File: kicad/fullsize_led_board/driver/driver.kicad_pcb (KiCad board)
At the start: 2 copper layers, 163.5 x 127.5 mm, 131 parts, among them J4 Anodes Header, J5 Cathodes Header, Q1 SQ2351CES, Q10 SQ2351CES, Q11 SQ2351CES, Q12 SQ2351CES, Q13 SQ2351CES, Q14 SQ2351CES, Q15 SQ2351CES, Q16 SQ2351CES, Q17 SQ2351CES, Q18 SQ2351CES, Q19 SQ2351CES, Q2 SQ2351CES, Q20 SQ2351CES, Q21 SQ2351CES, Q22 SQ2351CES, Q23 SQ2351CES, Q24 SQ2351CES, Q3 SQ2351CES, Q4 SQ2351CES, Q5 SQ2351CES, Q6 SQ2351CES, Q7 SQ2351CES, Q8 SQ2351CES, Q9 SQ2351CES, U1 74HCT541, U2 74HCT595, U3 74HCT595, U4 74HCT595, U5 TPIC6B595N, U6 TPIC6B595N, U7 TPIC6B595N, U8 TPIC6B595N

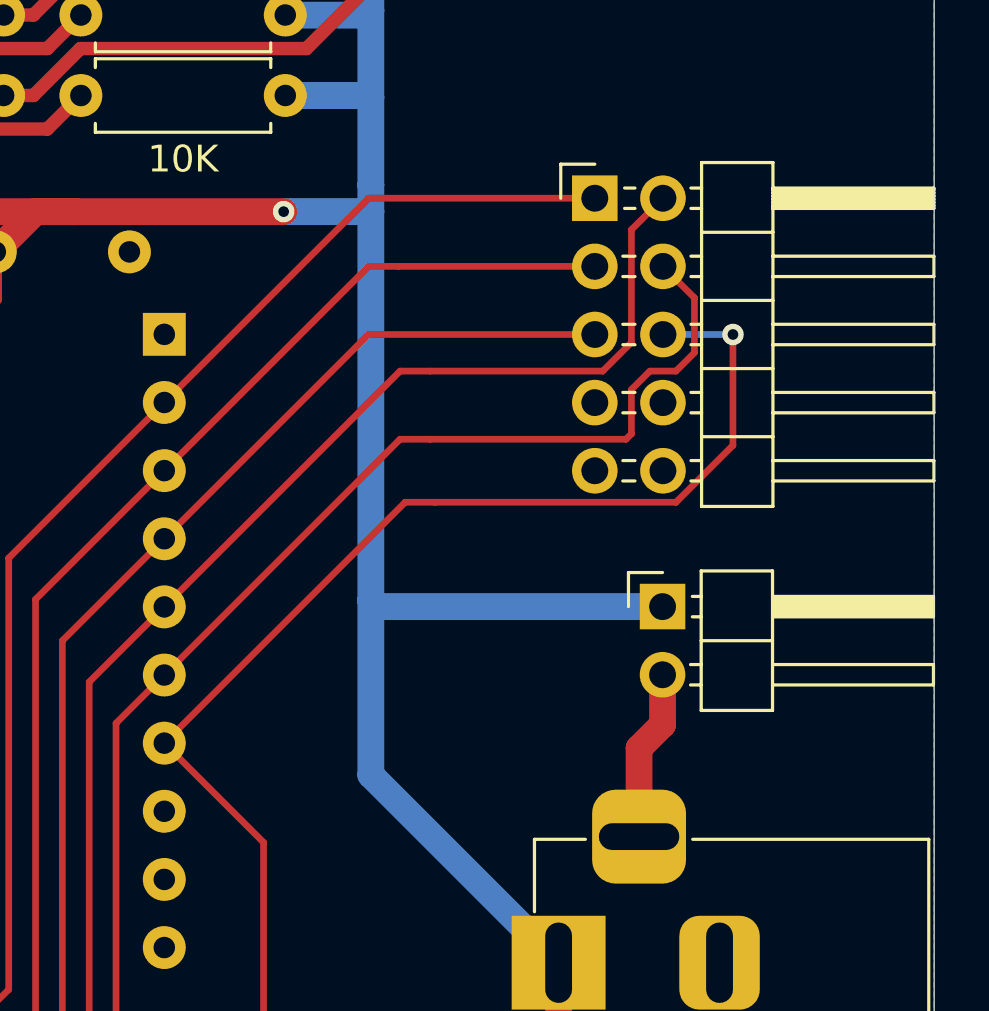
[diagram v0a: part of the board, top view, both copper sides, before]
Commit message: fullsize led board: done, inspection now and then ordering
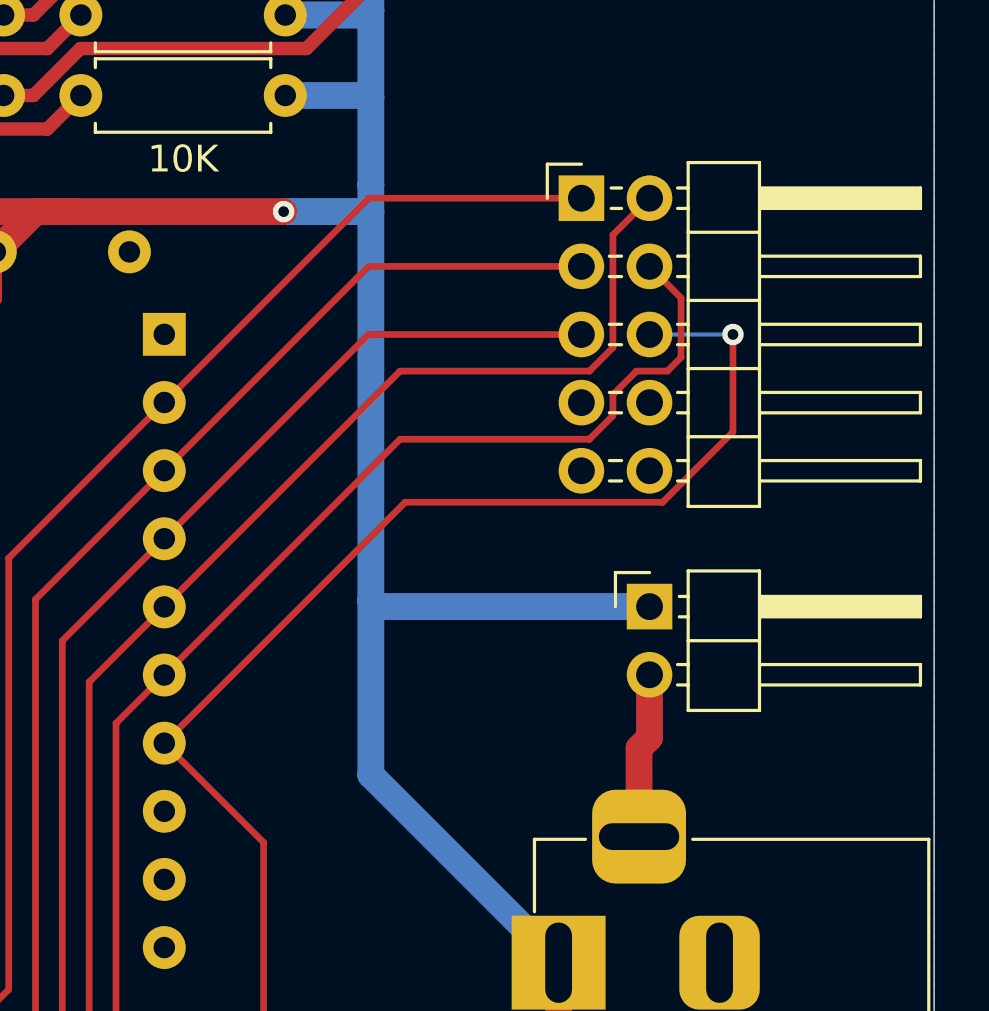
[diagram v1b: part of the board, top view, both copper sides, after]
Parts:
- moved J3 0.50 mm to (246.8, 108.5)
- moved J1 0.49 mm to (249.4, 123.7)
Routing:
- net ShiftRowStrobe: track 48.4 -> 47.5 mm
- net ShiftRowData: track 47.5 -> 47.0 mm
- net RowStrobe: track 48.5 -> 48.0 mm
- net RowData: track 51.3 -> 50.8 mm
- net ApplyRowAndStrobe: track 43.7 -> 43.2 mm
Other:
- board text added: "${REVISION} ~ ${ISSUE_DATE}"
- board text added: "FPGA Mediaplayer LED Board Driver"
- board text added: "Visit the project on github.com alpyen/fpga-mediaplayer"
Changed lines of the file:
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@@
 	(title_block
 		(title "Fullsize LED Board (Driver)")
+		(date "16.07.2024")
+		(rev "v1.0")
 	)
 	(layers
@@
 			(plot_on_all_layers_selection 0x0000000_00000000)
 			(disableapertmacros no)
-			(usegerberextensions no)
-			(usegerberattributes yes)
-			(usegerberadvancedattributes yes)
-			(creategerberjobfile yes)
+			(usegerberextensions yes)
+			(usegerberattributes no)
+			(usegerberadvancedattributes no)
+			(creategerberjobfile no)
 			(dashed_line_dash_ratio 12.000000)
 			(dashed_line_gap_ratio 3.000000)
@@
 			(plotinvisibletext no)
 			(sketchpadsonfab no)
-			(subtractmaskfromsilk no)
+			(subtractmaskfromsilk yes)
 			(outputformat 1)
 			(mirror no)
-			(drillshape 1)
+			(drillshape 0)
 			(scaleselection 1)
-			(outputdirectory "")
+			(outputdirectory "driver_plots/")
 		)
 	)
@@
 	(footprint "Connector_PinHeader_2.54mm:PinHeader_2x05_P2.54mm_Horizontal"
 		(layer "F.Cu")
-		(at 247.35 108.5)
+		(at 246.85 108.5)
 		(descr "Through hole angled pin header, 2x05, 2.54mm pitch, 6mm pin length, double rows")
 		(tags "Through hole angled pin header THT 2x05 2.54mm double row")
@@
 	(footprint "Connector_PinHeader_2.54mm:PinHeader_1x02_P2.54mm_Horizontal"
 		(layer "F.Cu")
-		(at 249.875 123.725)
+		(at 249.39 123.725)
 		(descr "Through hole angled pin header, 1x02, 2.54mm pitch, 6mm pin length, single row")
 		(tags "Through hole angled pin header THT 1x02 2.54mm single row")
@@
 		(layer "Edge.Cuts")
 	)
+	(gr_text "Visit the project on github.com\nalpyen/fpga-mediaplayer"
+		(at 150 82.5 -0)
+		(layer "B.SilkS")
+		(effects
+			(font
+				(size 2 2)
+				(thickness 0.3)
+			)
+			(justify mirror)
+		)
+	)
+	(gr_text "FPGA Mediaplayer\nLED Board Driver"
+		(at 150 67.5 -0)
+		(layer "B.SilkS" knockout)
+		(effects
+			(font
+				(size 3 3)
+				(thickness 0.5)
+				(bold yes)
+			)
+			(justify bottom mirror)
+		)
+	)
+	(gr_text "${REVISION} ~ ${ISSUE_DATE}"
+		(at 150 70 -0)
+		(layer "B.SilkS")
+		(effects
+			(font
+				(size 2 2)
+				(thickness 0.4)
+				(bold yes)
+			)
+			(justify top mirror)
+		)
+	)
 	(segment
 		(start 182.7 116.115)
@@
 	)
 	(segment
-		(start 249.875 123.725)
-		(end 239.225 123.725)
-		(width 1)
-		(layer "B.Cu")
-		(net 2)
-	)
-	(segment
 		(start 242.3625 87.36)
 		(end 240.5 87.36)
@@
 	)
 	(segment
+		(start 239.225 123.725)
+		(end 239 123.5)
+		(width 1)
+		(layer "B.Cu")
+		(net 2)
+	)
+	(segment
 		(start 235.81 104.67)
 		(end 238.92 104.67)
@@
 	)
 	(segment
+		(start 239.225 123.725)
+		(end 249.39 123.725)
+		(width 1)
+		(layer "B.Cu")
+		(net 2)
+	)
+	(segment
 		(start 112 130.055)
 		(end 112 117.415)
@@
 	)
 	(segment
-		(start 239.225 123.725)
-		(end 239 123.5)
-		(width 1)
-		(layer "B.Cu")
-		(net 2)
-	)
-	(segment
 		(start 235.81 95.67)
 		(end 238.92 95.67)
@@
 	)
 	(segment
-		(start 249.875 128.125)
-		(end 249 129)
+		(start 249.39 128.61)
+		(end 249.39 126.265)
 		(width 1)
 		(layer "F.Cu")
@@
 	)
 	(segment
-		(start 249.875 126.265)
-		(end 249.875 128.125)
+		(start 249 132.3)
+		(end 249 129)
 		(width 1)
 		(layer "F.Cu")
@@
 	(segment
 		(start 249 129)
-		(end 249 132.3)
+		(end 249.39 128.61)
 		(width 1)
 		(layer "F.Cu")
@@
 	)
 	(segment
-		(start 227.5 142)
-		(end 227.5 124.995)
+		(start 238.915 113.58)
+		(end 231.3 121.195)
 		(width 0.25)
 		(layer "F.Cu")
@@
 	)
 	(segment
-		(start 227.5 124.995)
-		(end 231.3 121.195)
+		(start 227.5 142)
+		(end 227.5 124.995)
 		(width 0.25)
 		(layer "F.Cu")
@@
 	)
 	(segment
-		(start 226 143.5)
-		(end 227.5 142)
+		(start 246.85 113.58)
+		(end 238.915 113.58)
 		(width 0.25)
 		(layer "F.Cu")
@@
 	)
 	(segment
-		(start 238.915 113.58)
-		(end 247.35 113.58)
+		(start 227.5 124.995)
+		(end 231.3 121.195)
 		(width 0.25)
 		(layer "F.Cu")
@@
 	)
 	(segment
-		(start 231.3 121.195)
-		(end 238.915 113.58)
+		(start 226 143.5)
+		(end 227.5 142)
 		(width 0.25)
 		(layer "F.Cu")
@@
 	)
 	(segment
-		(start 229.5 128.075)
-		(end 231.3 126.275)
+		(start 247.146701 117.485)
+		(end 240.09 117.485)
 		(width 0.25)
 		(layer "F.Cu")
@@
 	)
 	(segment
-		(start 251.065 112.215)
-		(end 251.065 114.256701)
+		(start 229.5 128.075)
+		(end 231.3 126.275)
 		(width 0.25)
 		(layer "F.Cu")
@@
 	(segment
 		(start 240.09 117.485)
-		(end 241.2 117.485)
-		(width 0.25)
-		(layer "F.Cu")
-		(net 7)
-	)
-	(segment
-		(start 251.065 114.256701)
-		(end 250.376701 114.945)
+		(end 231.3 126.275)
 		(width 0.25)
 		(layer "F.Cu")
@@
 	)
 	(segment
-		(start 231.3 126.275)
-		(end 240.09 117.485)
+		(start 250.565 114.435)
+		(end 250.055 114.945)
 		(width 0.25)
 		(layer "F.Cu")
@@
 	)
 	(segment
-		(start 249.89 111.04)
-		(end 251.065 112.215)
+		(start 248.025 115.823299)
+		(end 248.025 116.606701)
 		(width 0.25)
 		(layer "F.Cu")
@@
 	)
 	(segment
-		(start 248.715 115.633299)
-		(end 248.715 117.284999)
+		(start 248.025 116.606701)
+		(end 247.146701 117.485)
 		(width 0.25)
 		(layer "F.Cu")
@@
 	)
 	(segment
-		(start 249.403299 114.945)
-		(end 248.715 115.633299)
+		(start 250.565 112.215)
+		(end 250.565 114.435)
 		(width 0.25)
 		(layer "F.Cu")
@@
 	)
 	(segment
-		(start 248.715 117.284999)
-		(end 248.514999 117.485)
+		(start 248.903299 114.945)
+		(end 248.025 115.823299)
 		(width 0.25)
 		(layer "F.Cu")
@@
 	)
 	(segment
-		(start 250.376701 114.945)
-		(end 249.403299 114.945)
+		(start 232 143.5)
+		(end 229.5 141)
 		(width 0.25)
 		(layer "F.Cu")
@@
 	)
 	(segment
-		(start 232 143.5)
-		(end 229.5 141)
+		(start 249.39 111.04)
+		(end 250.565 112.215)
 		(width 0.25)
 		(layer "F.Cu")
@@
 	)
 	(segment
-		(start 248.514999 117.485)
-		(end 241.2 117.485)
+		(start 250.055 114.945)
+		(end 248.903299 114.945)
 		(width 0.25)
 		(layer "F.Cu")
@@
 	)
 	(segment
-		(start 223 143.5)
-		(end 226.5 140)
+		(start 238.915 111.04)
+		(end 246.85 111.04)
 		(width 0.25)
 		(layer "F.Cu")
@@
 	)
 	(segment
-		(start 226.5 140)
-		(end 226.5 123.455)
+		(start 223 143.5)
+		(end 226.5 140)
 		(width 0.25)
 		(layer "F.Cu")
@@
 	)
 	(segment
-		(start 247.35 111.04)
-		(end 240.025 111.04)
+		(start 226.5 140)
+		(end 226.5 123.455)
 		(width 0.25)
 		(layer "F.Cu")
@@
 	)
 	(segment
-		(start 238.915 111.04)
-		(end 240.025 111.04)
-		(width 0.25)
-		(layer "F.Cu")
-		(net 167)
-	)
-	(segment
 		(start 225.5 121.915)
 		(end 231.3 116.115)
@@
 	(segment
 		(start 238.915 108.5)
-		(end 247.35 108.5)
+		(end 246.85 108.5)
 		(width 0.25)
 		(layer "F.Cu")
@@
 	)
 	(segment
-		(start 241.39 119.835)
-		(end 250.376701 119.835)
+		(start 240.28 119.835)
+		(end 249.876701 119.835)
 		(width 0.25)
 		(layer "F.Cu")
@@
 	)
 	(segment
-		(start 252.5 117.711701)
+		(start 252.5 117.211701)
 		(end 252.5 113.58)
 		(width 0.25)
@@
 	)
 	(segment
-		(start 240.28 119.835)
-		(end 241.39 119.835)
-		(width 0.25)
-		(layer "F.Cu")
-		(net 169)
-	)
-	(segment
-		(start 250.376701 119.835)
-		(end 252.5 117.711701)
+		(start 249.876701 119.835)
+		(end 252.5 117.211701)
 		(width 0.25)
 		(layer "F.Cu")
@@
 	)
 	(segment
-		(start 249.89 113.58)
-		(end 252.5 113.58)
-		(width 0.25)
-		(layer "B.Cu")
-		(net 169)
-	)
-	(segment
 		(start 252.42 113.58)
 		(end 252.5 113.5)
@@
 	)
 	(segment
-		(start 249.89 108.5)
-		(end 248.715 109.675)
-		(width 0.25)
-		(layer "F.Cu")
-		(net 170)
+		(start 249.39 113.58)
+		(end 252.5 113.58)
+		(width 0.15)
+		(layer "B.Cu")
+		(net 169)
 	)
 	(segment
@@
 	)
 	(segment
-		(start 229 143.5)
-		(end 229 142)
+		(start 248.025 114.066701)
+		(end 247.146701 114.945)
 		(width 0.25)
 		(layer "F.Cu")
@@
 	)
 	(segment
-		(start 248.715 113.876701)
-		(end 247.646701 114.945)
+		(start 229 143.5)
+		(end 229 142)
 		(width 0.25)
 		(layer "F.Cu")
@@
 	)
 	(segment
-		(start 231.3 123.735)
-		(end 240.09 114.945)
+		(start 240.09 114.945)
+		(end 231.3 123.735)
 		(width 0.25)
 		(layer "F.Cu")
@@
 	)
 	(segment
-		(start 247.646701 114.945)
-		(end 241.2 114.945)
+		(start 249.39 108.5)
+		(end 248.025 109.865)
 		(width 0.25)
 		(layer "F.Cu")
@@
 	)
 	(segment
-		(start 228.5 141.5)
-		(end 228.5 126.535)
+		(start 247.146701 114.945)
+		(end 240.09 114.945)
 		(width 0.25)
 		(layer "F.Cu")
@@
 	)
 	(segment
-		(start 240.09 114.945)
-		(end 241.2 114.945)
+		(start 248.025 109.865)
+		(end 248.025 114.066701)
 		(width 0.25)
 		(layer "F.Cu")
@@
 	)
 	(segment
-		(start 248.715 109.675)
-		(end 248.715 113.876701)
+		(start 228.5 141.5)
+		(end 228.5 126.535)
 		(width 0.25)
 		(layer "F.Cu")

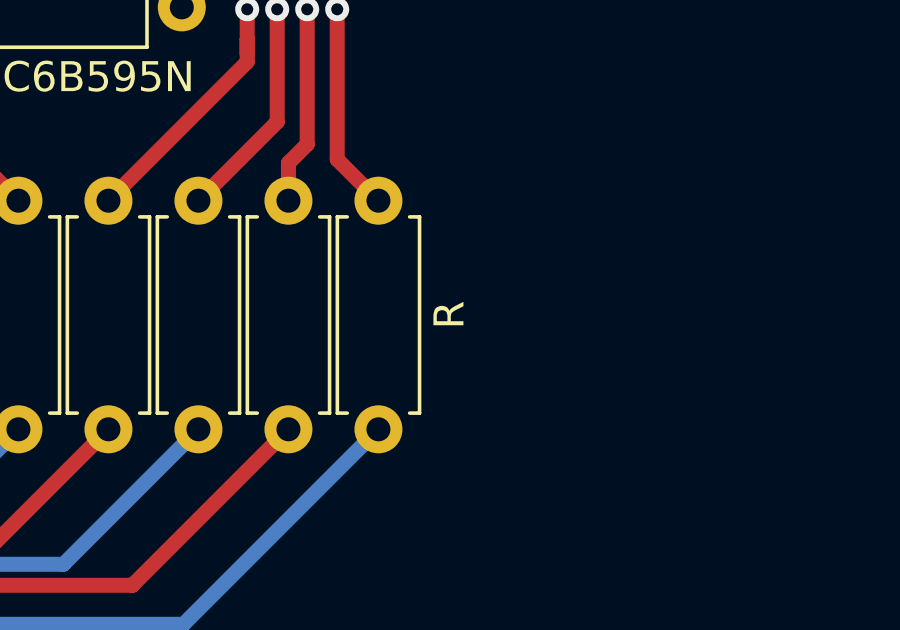
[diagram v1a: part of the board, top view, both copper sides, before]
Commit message: kicad: finalized led resistor values
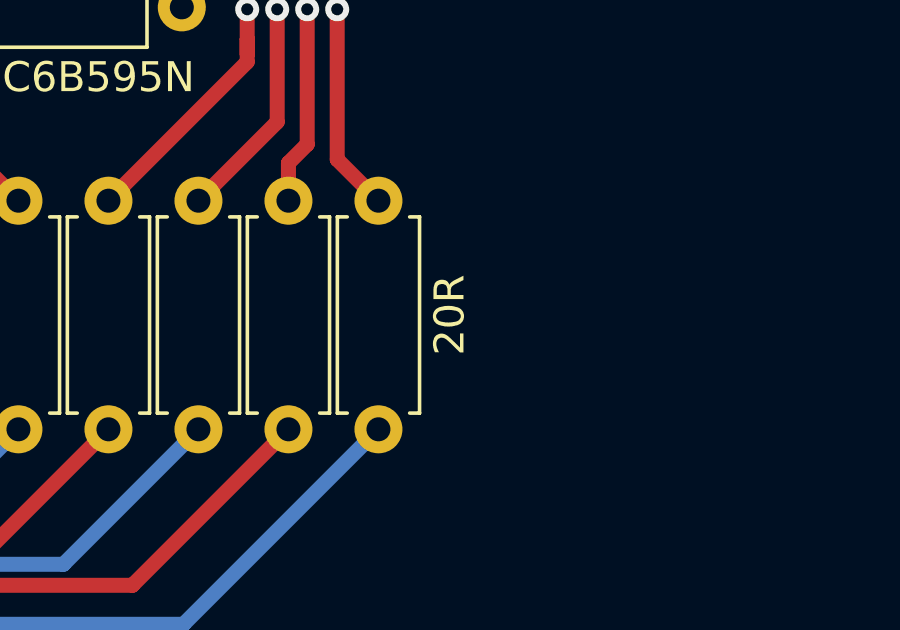
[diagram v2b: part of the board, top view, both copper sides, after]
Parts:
- R55, R56, R57, R58, R59, R60, R61, R62, R63, R64, R65, R66, R67, R68, R69, R70, R71, R72, R73, R74, R75, R76, R77, R78, R79, R80, R81, R82, R83, R84, R85, R86: value R -> 20R
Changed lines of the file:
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@@
 			)
 		)
-		(property "Value" "R"
+		(property "Value" "20R"
 			(at 3.81 2.37 90)
 			(layer "F.Fab")
@@
 			)
 		)
-		(property "Value" "R"
+		(property "Value" "20R"
 			(at 3.81 2.37 90)
 			(layer "F.Fab")
@@
 			)
 		)
-		(property "Value" "R"
+		(property "Value" "20R"
 			(at 3.81 2.37 90)
 			(layer "F.Fab")
@@
 			)
 		)
-		(property "Value" "R"
+		(property "Value" "20R"
 			(at 3.81 2.37 90)
 			(layer "F.Fab")
@@
 			)
 		)
-		(property "Value" "R"
+		(property "Value" "20R"
 			(at 3.81 2.37 90)
 			(layer "F.Fab")
@@
 			)
 		)
-		(property "Value" "R"
+		(property "Value" "20R"
 			(at 3.81 2.37 90)
 			(layer "F.Fab")
@@
 			)
 		)
-		(property "Value" "R"
+		(property "Value" "20R"
 			(at 3.81 2.37 90)
 			(layer "F.Fab")
@@
 			)
 		)
-		(property "Value" "R"
+		(property "Value" "20R"
 			(at 3.81 2.37 90)
 			(layer "F.Fab")
@@
 			)
 		)
-		(property "Value" "R"
+		(property "Value" "20R"
 			(at 3.81 2.37 90)
 			(layer "F.Fab")
@@
 			)
 		)
-		(property "Value" "R"
+		(property "Value" "20R"
 			(at 3.81 2.37 90)
 			(layer "F.Fab")
@@
 			)
 		)
-		(property "Value" "R"
+		(property "Value" "20R"
 			(at 3.81 2.37 90)
 			(layer "F.Fab")
@@
 			)
 		)
-		(property "Value" "R"
+		(property "Value" "20R"
 			(at 3.81 2.37 90)
 			(layer "F.Fab")
@@
 			)
 		)
-		(property "Value" "R"
+		(property "Value" "20R"
 			(at 3.81 2.37 90)
 			(layer "F.Fab")
@@
 			)
 		)
-		(property "Value" "R"
+		(property "Value" "20R"
 			(at 3.81 2.37 90)
 			(layer "F.Fab")
@@
 			)
 		)
-		(property "Value" "R"
+		(property "Value" "20R"
 			(at 3.81 2.37 90)
 			(layer "F.Fab")
@@
 			)
 		)
-		(property "Value" "R"
+		(property "Value" "20R"
 			(at 3.81 2.37 90)
 			(layer "F.Fab")
@@
 			)
 		)
-		(property "Value" "R"
+		(property "Value" "20R"
 			(at 3.81 2.37 90)
 			(layer "F.Fab")
@@
 			)
 		)
-		(property "Value" "R"
+		(property "Value" "20R"
 			(at 3.81 2.37 90)
 			(layer "F.Fab")
@@
 			)
 		)
-		(property "Value" "R"
+		(property "Value" "20R"
 			(at 3.81 2.37 90)
 			(layer "F.Fab")
@@
 			)
 		)
-		(property "Value" "R"
+		(property "Value" "20R"
 			(at 3.81 2.37 90)
 			(layer "F.Fab")
@@
 			)
 		)
-		(property "Value" "R"
+		(property "Value" "20R"
 			(at 3.81 2.37 90)
 			(layer "F.Fab")
@@
 			)
 		)
-		(property "Value" "R"
+		(property "Value" "20R"
 			(at 3.81 2.37 90)
 			(layer "F.Fab")
@@
 			)
 		)
-		(property "Value" "R"
+		(property "Value" "20R"
 			(at 3.81 2.37 90)
 			(layer "F.SilkS")
@@
 			)
 		)
-		(property "Value" "R"
+		(property "Value" "20R"
 			(at 3.81 2.37 90)
 			(layer "F.Fab")
@@
 			)
 		)
-		(property "Value" "R"
+		(property "Value" "20R"
 			(at 3.81 2.37 90)
 			(layer "F.Fab")
@@
 			)
 		)
-		(property "Value" "R"
+		(property "Value" "20R"
 			(at 3.81 2.37 90)
 			(layer "F.Fab")
@@
 			)
 		)
-		(property "Value" "R"
+		(property "Value" "20R"
 			(at 3.81 2.37 90)
 			(layer "F.Fab")
@@
 			)
 		)
-		(property "Value" "R"
+		(property "Value" "20R"
 			(at 3.81 2.37 90)
 			(layer "F.Fab")
@@
 			)
 		)
-		(property "Value" "R"
+		(property "Value" "20R"
 			(at 3.81 2.37 90)
 			(layer "F.Fab")
@@
 			)
 		)
-		(property "Value" "R"
+		(property "Value" "20R"
 			(at 3.81 2.37 90)
 			(layer "F.Fab")
@@
 			)
 		)
-		(property "Value" "R"
+		(property "Value" "20R"
 			(at 3.81 2.37 90)
 			(layer "F.Fab")
@@
 			)
 		)
-		(property "Value" "R"
+		(property "Value" "20R"
 			(at 3.81 2.37 90)
 			(layer "F.Fab")
